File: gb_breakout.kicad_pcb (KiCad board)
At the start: 2 copper layers, 51 x 60.7 mm, 14 parts, among them IC1 74ALVC164245DGG_11, IC2 74ALVC164245DGG_11, J1 Conn_02x16_Counter_Clockwise, U1 Cartridge_Bus

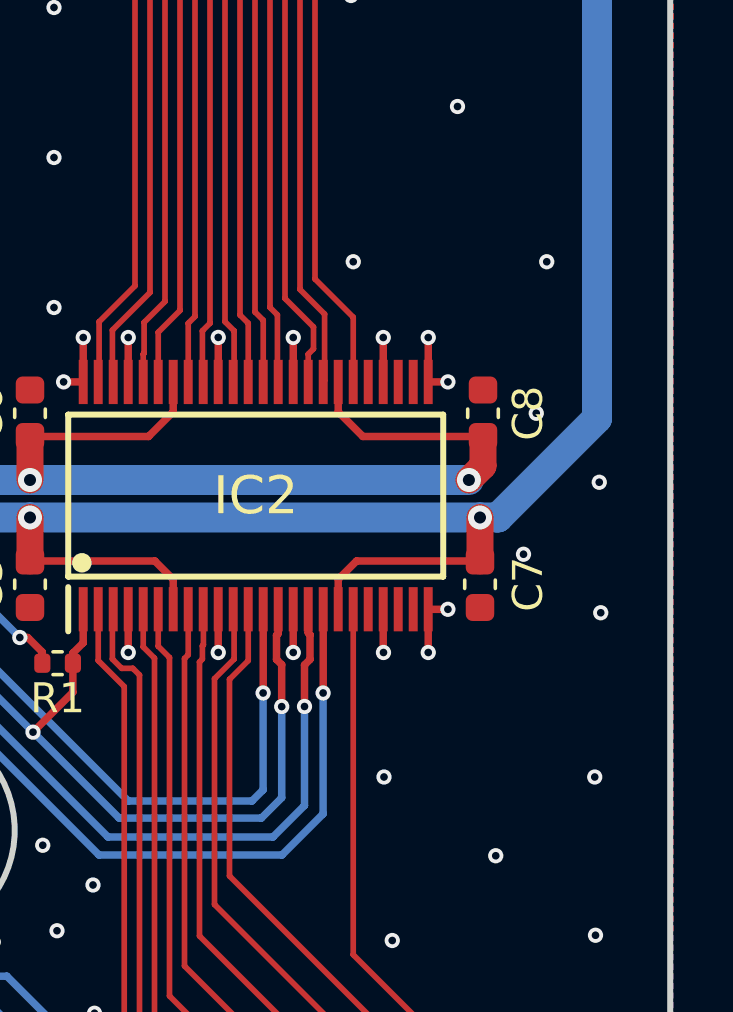
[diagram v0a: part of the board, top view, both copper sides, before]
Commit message: add pulldown resistors to floating transciever pins, update render, update BOM
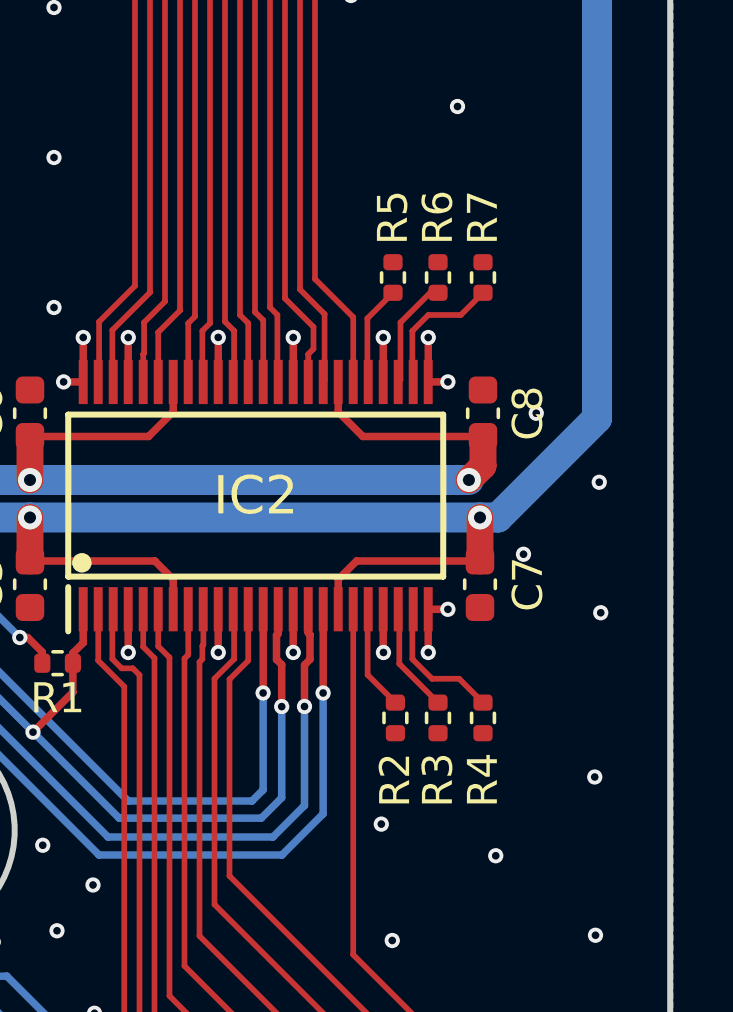
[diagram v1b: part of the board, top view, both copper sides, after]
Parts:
- added R2: 1k, Resistor_SMD:R_0402_1005Metric, F.Cu at (158.6, 103.9)
- added R3: 1k, Resistor_SMD:R_0402_1005Metric, F.Cu at (160.0, 103.9)
- added R4: 1k, Resistor_SMD:R_0402_1005Metric, F.Cu at (161.5, 103.9)
- added R5: 1k, Resistor_SMD:R_0402_1005Metric, F.Cu at (158.5, 89.2)
- added R6: 1k, Resistor_SMD:R_0402_1005Metric, F.Cu at (160.0, 89.2)
- added R7: 1k, Resistor_SMD:R_0402_1005Metric, F.Cu at (161.5, 89.2)
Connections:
- IC2 pad 20: unconnected-(IC2-Pad20) -> Net-(IC2-Pad20)
- IC2 pad 22: unconnected-(IC2-Pad22) -> Net-(IC2-Pad22)
- IC2 pad 23: unconnected-(IC2-Pad23) -> Net-(IC2-Pad23)
- IC2 pad 26: unconnected-(IC2-Pad26) -> Net-(IC2-Pad26)
- IC2 pad 27: unconnected-(IC2-Pad27) -> Net-(IC2-Pad27)
- IC2 pad 29: unconnected-(IC2-Pad29) -> Net-(IC2-Pad29)
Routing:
- net Net-(IC2-Pad23): track 0.00 -> 4.63 mm
- net Net-(IC2-Pad26): track 0.00 -> 4.59 mm
- net Net-(IC2-Pad27): track 0.00 -> 3.67 mm
- net Net-(IC2-Pad22): track 0.00 -> 3.66 mm
- net Net-(IC2-Pad20): track 0.00 -> 3.50 mm
- net Net-(IC2-Pad29): track 0.00 -> 3.34 mm
- net GND: vias 105 -> 103

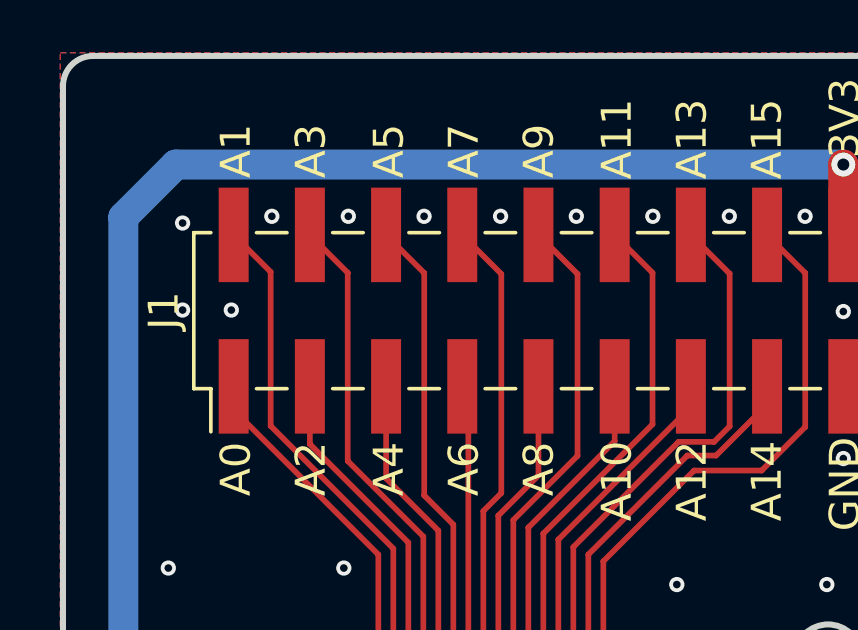
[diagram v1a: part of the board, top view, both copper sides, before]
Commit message: replace bus transciever with SN74LVC16T245 to remove power sequencing requirement
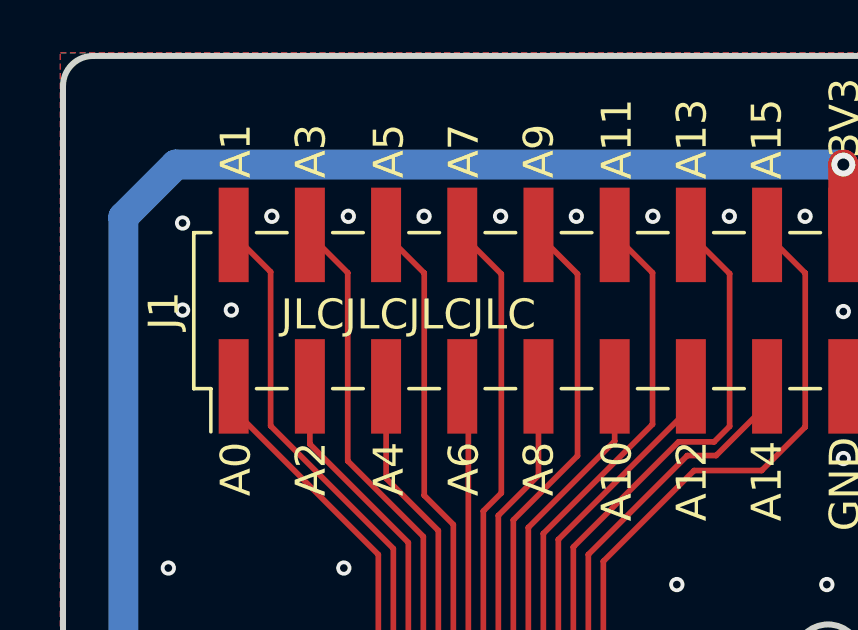
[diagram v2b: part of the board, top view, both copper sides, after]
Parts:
- IC1, IC2: value 74ALVC164245DGG_11 -> 74LVC16T245DGGRG4; footprint 74ALVC164245DGG_11:SOP50P810X120-48N -> 74LVC16T245DGGRG4:SOP50P810X120-48N
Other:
- board text added: "JLCJLCJLCJLC"

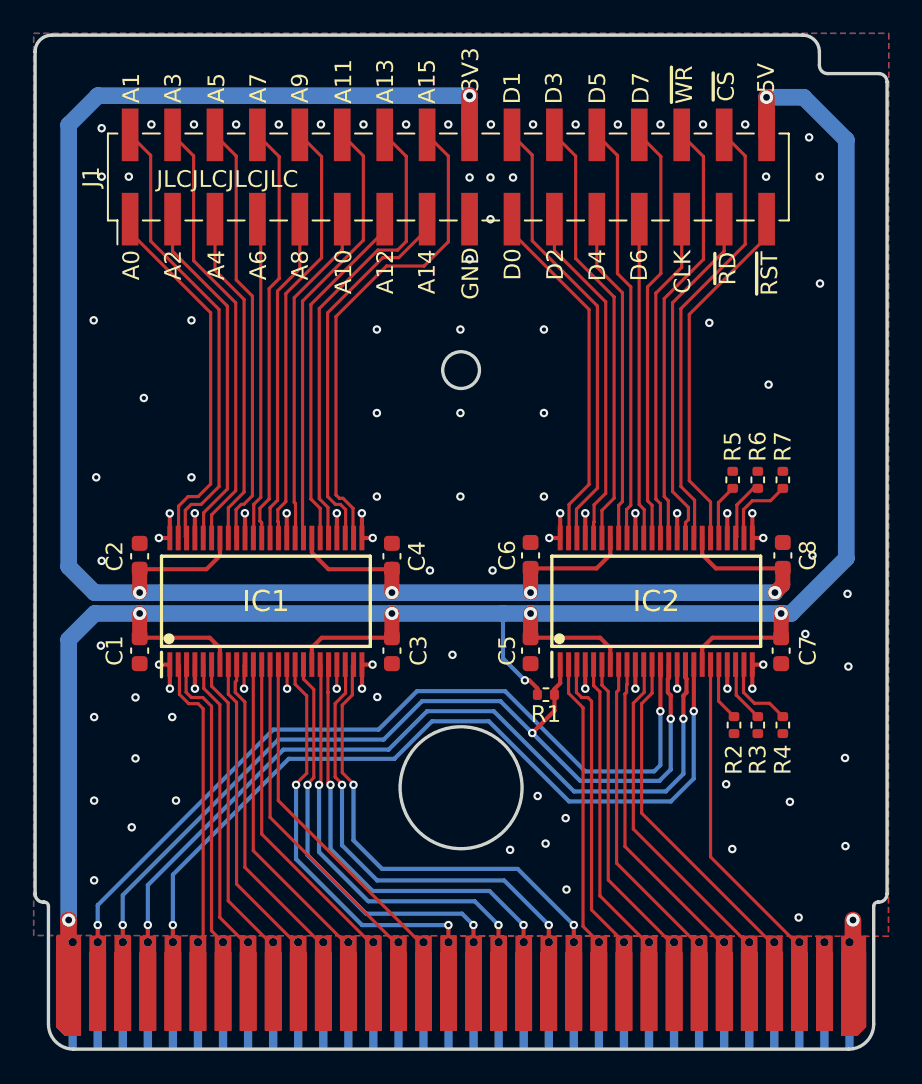
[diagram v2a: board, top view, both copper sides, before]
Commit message: OE on 2nd bus transciever now connected to A15, isolates data bus from the cartridge when GB is not accessing the cartridge specifically (ROM reads only at the moment)
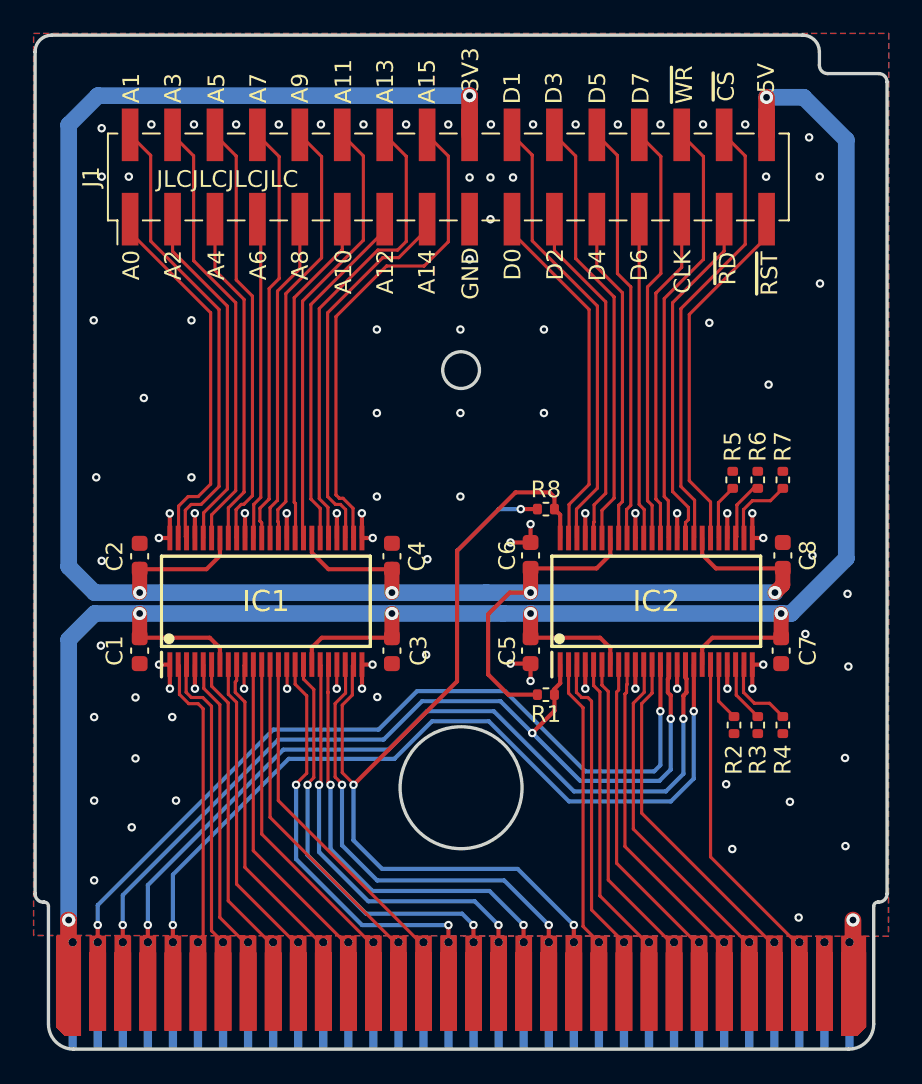
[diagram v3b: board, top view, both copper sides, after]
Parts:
- added R8: 1k, Resistor_SMD:R_0402_1005Metric, F.Cu at (147.3, 91.0)
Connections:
- IC2 pad 48: GND -> GB_A15
- R1 pad 2: +5V -> +3V3
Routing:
- net GB_A15: track 27.4 -> 54.0 mm
- net +3V3: track 126.9 -> 147.0 mm, vias 5 -> 6
- net +5V: track 135.7 -> 129.8 mm, vias 7 -> 6
- net GND: track 39.8 -> 42.2 mm, vias 103 -> 98

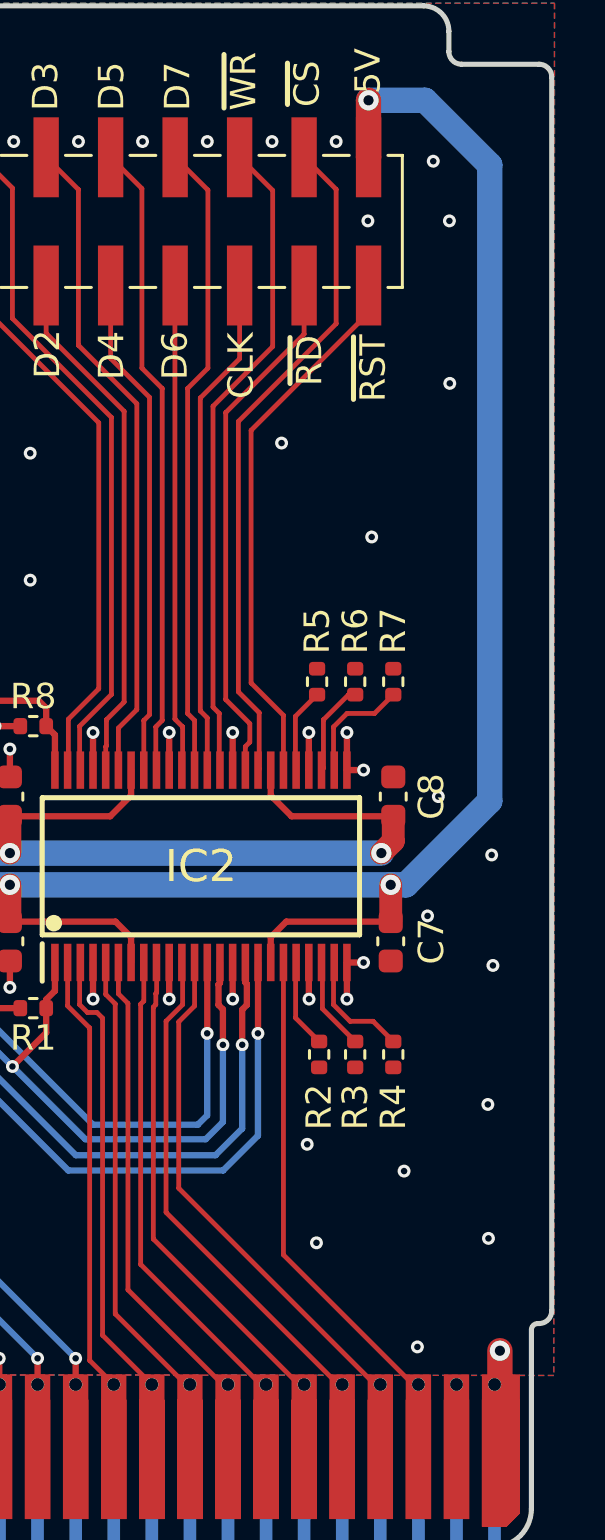
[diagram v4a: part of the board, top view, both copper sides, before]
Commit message: route open drain buffer on PCB
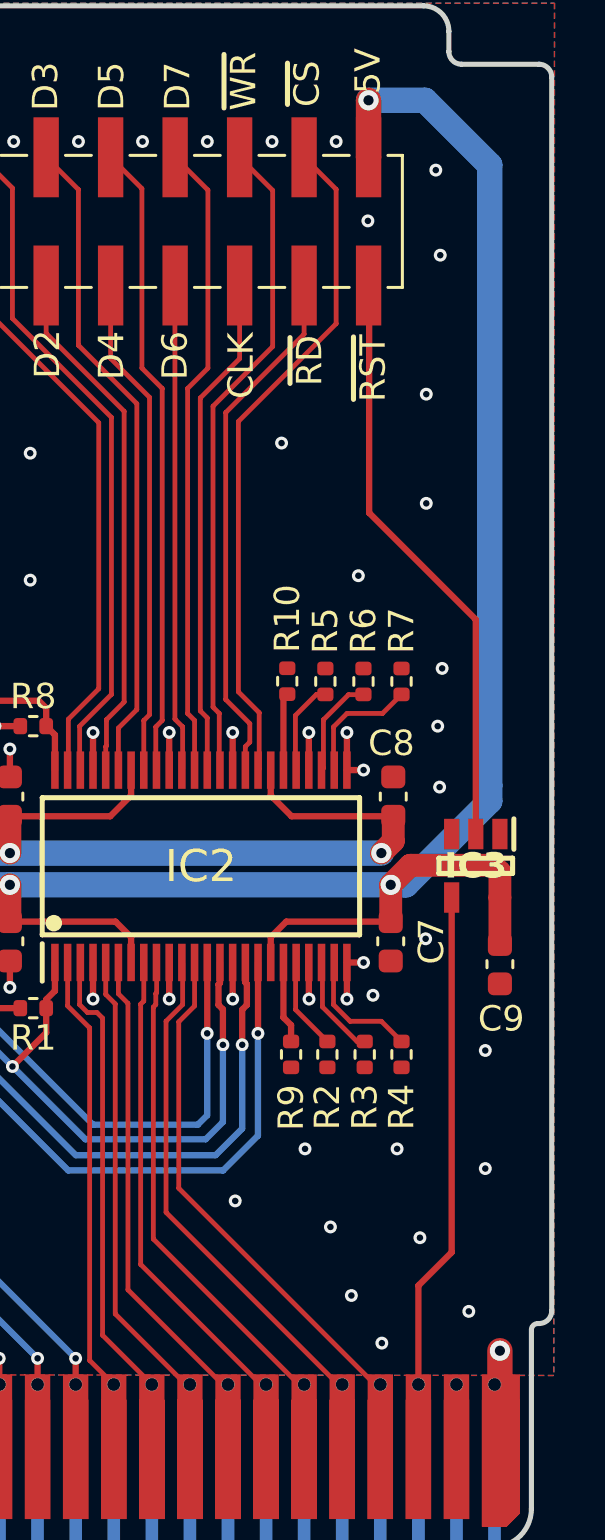
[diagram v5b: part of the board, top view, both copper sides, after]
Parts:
- added C9: 100n, Capacitor_SMD:C_0603_1608Metric, F.Cu at (165.7, 100.4)
- added IC3: SN74LVC1G07DBVT, SN74LVC1G07DBVT:SOT95P280X145-5N, F.Cu at (164.8, 96.5)
- added R10: 1k, Resistor_SMD:R_0402_1005Metric, F.Cu at (157.3, 89.2)
- added R9: 1k, Resistor_SMD:R_0402_1005Metric, F.Cu at (157.5, 103.9)
- moved R3 0.38 mm to (160.4, 103.9)
- moved R5 0.33 mm to (158.8, 89.2)
- moved R6 0.33 mm to (160.3, 89.2)
- moved R7 0.33 mm to (161.8, 89.2)
- moved R2 0.32 mm to (158.9, 103.9)
- moved R4 0.32 mm to (161.8, 103.9)
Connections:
- IC2 pad 19: GB_~{RST} -> Net-(IC2-2B5)
- IC2 pad 30: BO_~{RST} -> Net-(IC2-2A5)
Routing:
- net +5V: track 129.8 -> 137.4 mm
- net Net-(IC2-2B5): track 0.00 -> 3.24 mm
- net Net-(IC2-2A5): track 0.00 -> 3.05 mm
- net BO_~{RST}: track 21.5 -> 23.4 mm
- net GB_~{RST}: track 18.9 -> 19.7 mm
- net GND: vias 98 -> 104
